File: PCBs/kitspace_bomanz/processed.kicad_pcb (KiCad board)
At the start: 2 copper layers, 65 x 30 mm, 20 parts, among them U1 ADC08200CIMT

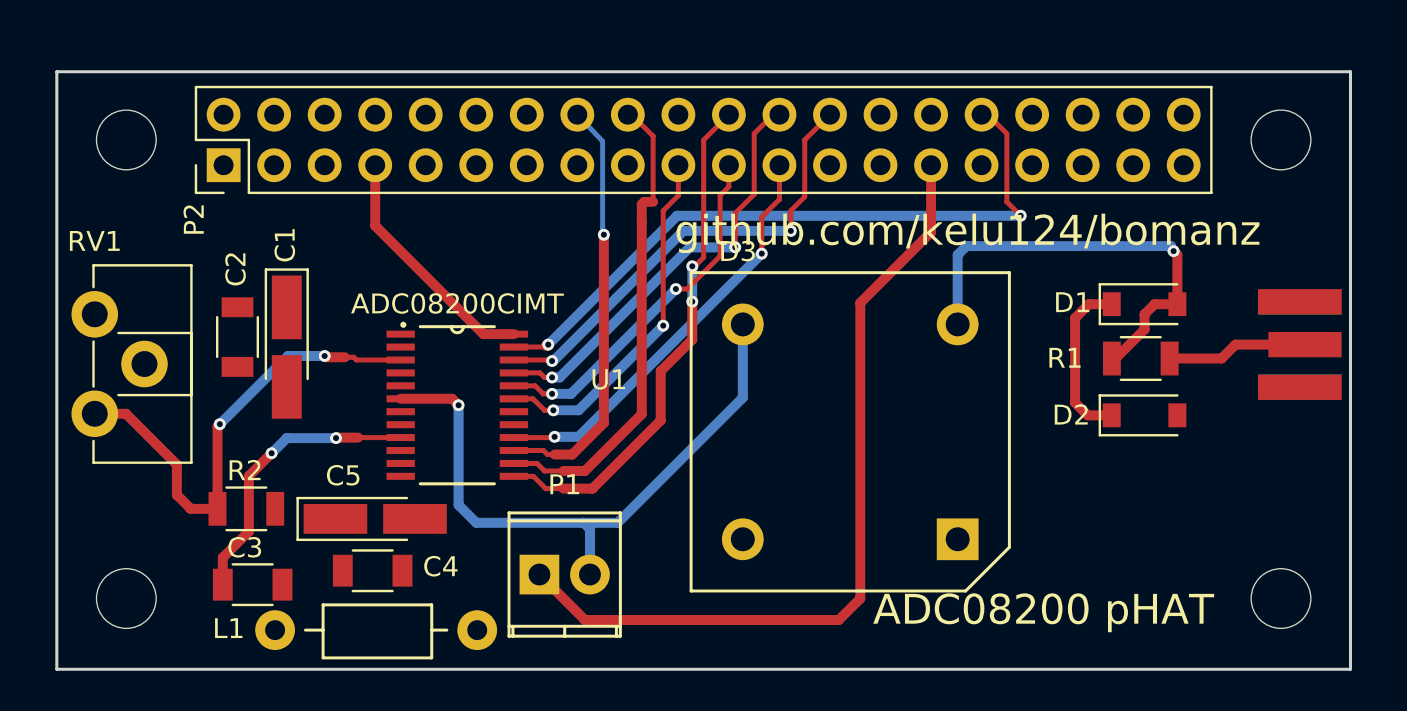
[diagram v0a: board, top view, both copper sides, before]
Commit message: recheck all circuits and clean up fill zone by rerouting the nets using freerouting and manually
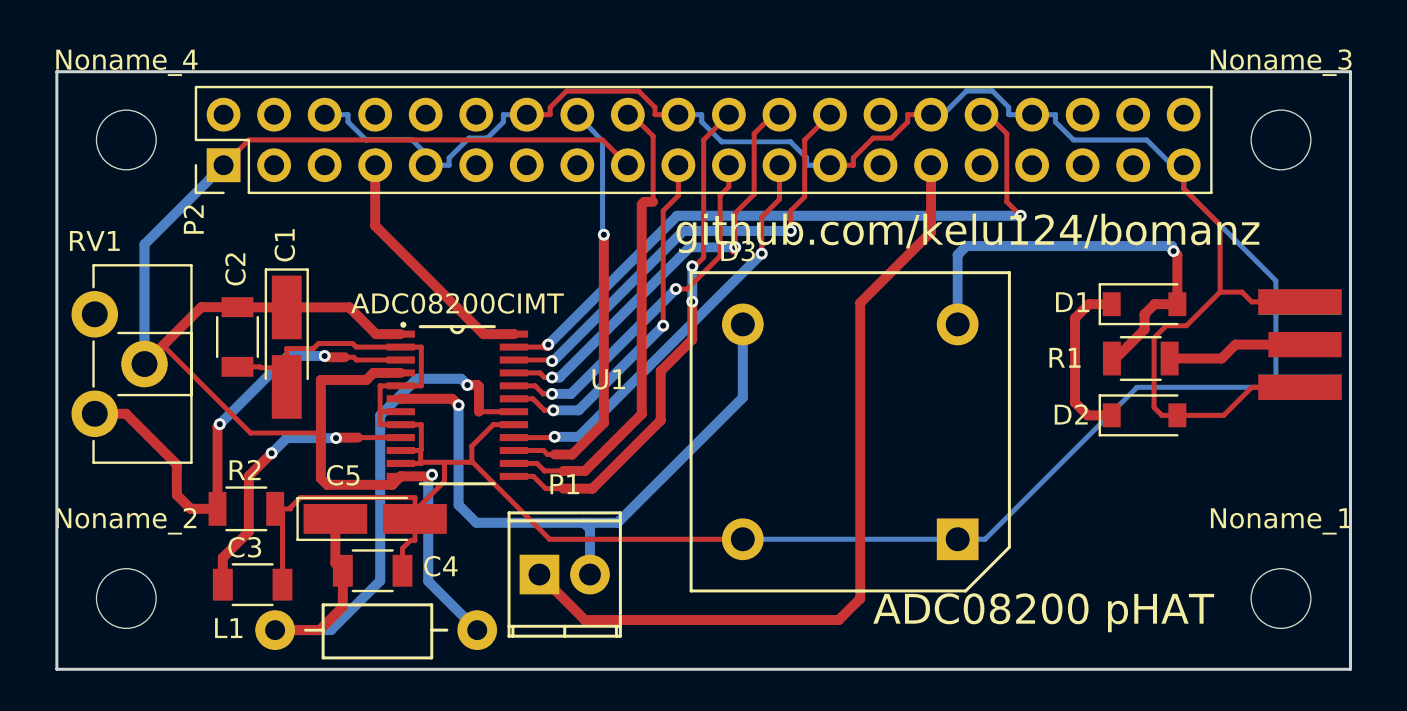
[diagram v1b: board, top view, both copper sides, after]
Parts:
- gave numbers to parts that had none: 5
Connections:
- C1 pad 1: (no net) -> +3V3
- C1 pad 2: (no net) -> GND
- C2 pad 1: (no net) -> +3V3
- C2 pad 2: (no net) -> GND
- C3 pad 2: (no net) -> GND
- C4 pad 1: (no net) -> Net-(C4-Pad1)
- C4 pad 2: (no net) -> GND
- C5 pad 1: (no net) -> Net-(C4-Pad1)
- C5 pad 2: (no net) -> GND
- D2 pad 2: (no net) -> GND
- D3 pad 2: (no net) -> GND
- D3 pad 3: (no net) -> GND
- L1 pad 1: (no net) -> +3V3
- L1 pad 2: (no net) -> Net-(C4-Pad1)
- Noname_5 pad 2: (no net) -> GND
- P2 pad 1: (no net) -> +3V3
- P2 pad 10: (no net) -> Net-(P2-Pad10)
- P2 pad 11: (no net) -> Net-(P2-Pad11)
- P2 pad 12: (no net) -> Net-(P2-Pad12)
- P2 pad 13: (no net) -> Net-(P2-Pad13)
- P2 pad 14: (no net) -> GND
- P2 pad 15: (no net) -> Net-(P2-Pad15)
- P2 pad 17: (no net) -> +3V3
- P2 pad 2: (no net) -> Net-(P2-Pad2)
- P2 pad 20: (no net) -> GND
- P2 pad 25: (no net) -> GND
- P2 pad 27: (no net) -> Net-(P2-Pad27)
- P2 pad 28: (no net) -> Net-(P2-Pad28)
- P2 pad 3: (no net) -> Net-(P2-Pad3)
- P2 pad 30: (no net) -> GND
- P2 pad 31: (no net) -> Net-(P2-Pad31)
- P2 pad 33: (no net) -> Net-(P2-Pad33)
- P2 pad 34: (no net) -> GND
- P2 pad 35: (no net) -> Net-(P2-Pad35)
- P2 pad 36: (no net) -> Net-(P2-Pad36)
- P2 pad 37: (no net) -> Net-(P2-Pad37)
- P2 pad 38: (no net) -> Net-(P2-Pad38)
- P2 pad 39: (no net) -> GND
- P2 pad 4: (no net) -> Net-(P2-Pad4)
- P2 pad 40: (no net) -> Net-(P2-Pad40)
- P2 pad 5: (no net) -> Net-(P2-Pad5)
- P2 pad 6: (no net) -> GND
- P2 pad 8: (no net) -> Net-(P2-Pad8)
- P2 pad 9: (no net) -> GND
- R2 pad 2: (no net) -> GND
- RV1 pad 2: (no net) -> +3V3
- U1 pad 1: (no net) -> +3V3
- U1 pad 10: (no net) -> GND
- U1 pad 11: (no net) -> GND
- U1 pad 12: (no net) -> +3V3
- U1 pad 17: (no net) -> GND
- U1 pad 18: (no net) -> Net-(C4-Pad1)
- U1 pad 2: (no net) -> GND
- U1 pad 4: (no net) -> +3V3
- U1 pad 5: (no net) -> GND
- U1 pad 7: (no net) -> GND
- U1 pad 8: (no net) -> GND
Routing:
- net GND: track 0.00 -> 190.3 mm
- net +3V3: track 0.00 -> 81.3 mm, vias 0 -> 1
- net Net-(C4-Pad1): track 0.00 -> 32.1 mm, vias 0 -> 1
